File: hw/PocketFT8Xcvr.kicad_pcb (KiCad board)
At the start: 4 copper layers, 101.6 x 69.9 mm, 55 parts, among them IC1 SI5351C-B-GM1, J1 HX8357D SPI, J2 22-23-2021, J3 22-23-2021, J5 HX8357D 8-BIT, Q1 2N3904, Q2 2N3906, Q3 2N7000, Q4 2N7000, U1 MCP3422A1T-E/SN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

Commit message: Initial routing complete
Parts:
- moved C1 7.64 mm to (177.0, 62.5)
- moved C2 1.84 mm to (168.9, 69.5)
- moved R3 1.84 mm to (163.8, 69.2)
- moved C4 1.29 mm to (174.0, 62.5)
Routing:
- net /SDA: track 143.8 -> 177.4 mm, vias 5 -> 8
- net /SCL: track 110.7 -> 141.1 mm, vias 5 -> 8
- net Net-(U2-AMI): track 0.00 -> 27.9 mm, vias 0 -> 2
- net Net-(TN1-20_A6_TX5_LRCLK1): track 0.00 -> 26.6 mm, vias 0 -> 1
- net Net-(U2-LOUT/[DFS]): track 0.00 -> 21.1 mm, vias 0 -> 2
- net GND: track 97.5 -> 110.1 mm, vias 24 -> 29
- net +3.3V: track 66.1 -> 74.5 mm, vias 9 -> 11
- net Net-(U2-DBYP): track 0.00 -> 4.84 mm

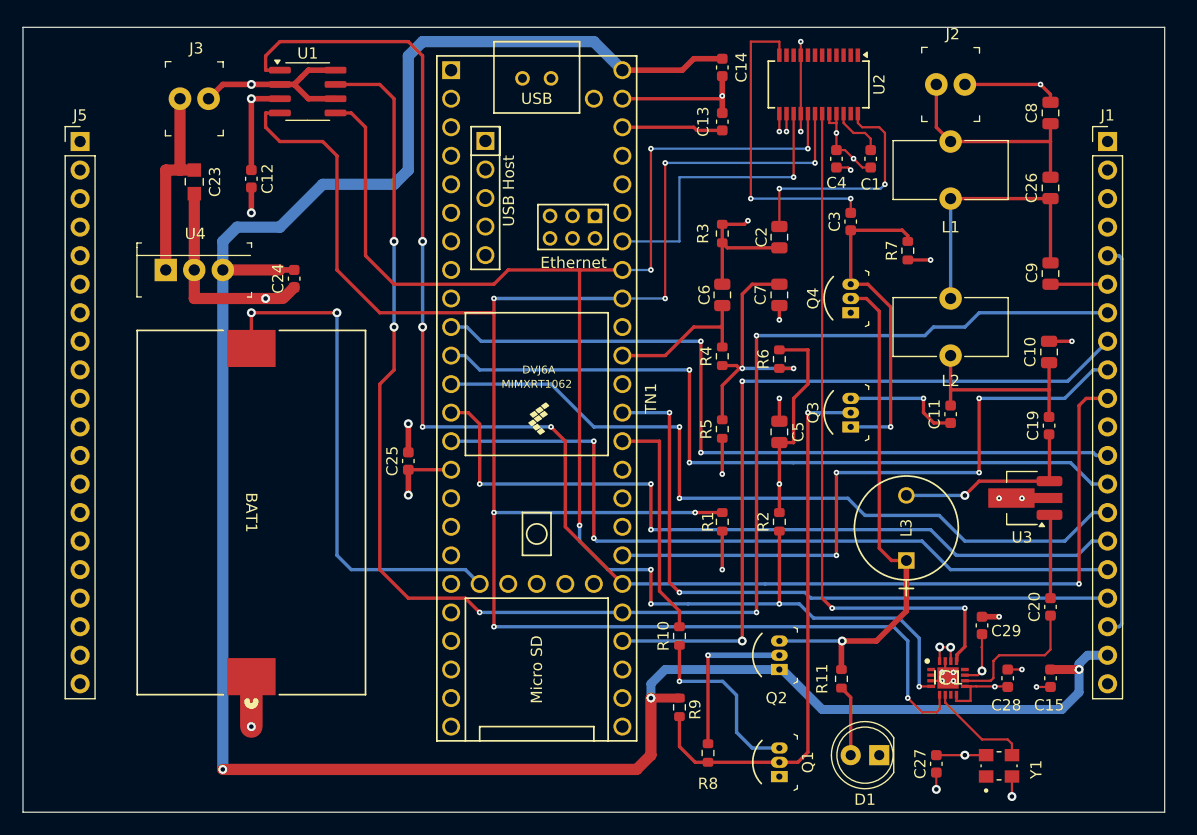
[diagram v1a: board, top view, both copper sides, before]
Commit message: Added GPS connector to board
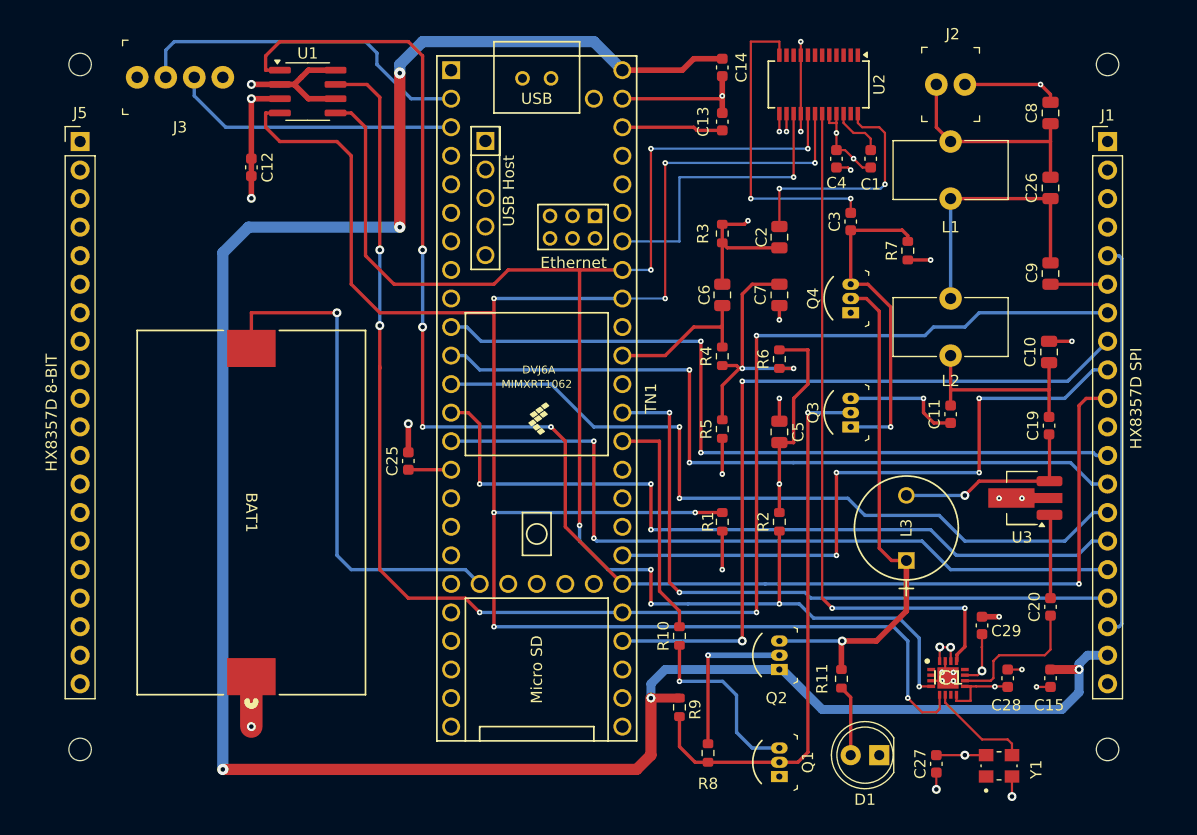
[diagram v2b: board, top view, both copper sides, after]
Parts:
- removed C23: 0.33UF, digikey-footprints:0805
- removed C24: 0.1UF, Capacitor_SMD:C_0603_1608Metric
- removed U4: L7805CV, digikey-footprints:TO-220-3
- added REF**: MountingHole_2mm, MountingHole:MountingHole_2mm, F.Cu at (106.7, 115.1)
- added REF**: MountingHole_2mm, MountingHole:MountingHole_2mm, F.Cu at (106.7, 54.1)
- added REF**: MountingHole_2mm, MountingHole:MountingHole_2mm, F.Cu at (198.1, 115.1)
- added REF**: MountingHole_2mm, MountingHole:MountingHole_2mm, F.Cu at (198.1, 54.1)
- J3: value 22-23-2021 -> GPS; footprint digikey-footprints:PinHeader_1x2_P2.54mm_Drill1.02mm -> digikey-footprints:PinHeader_1x4_P2.54mm_Drill1.02mm
- moved J3 4.26 mm to (111.8, 55.2)
- moved C12 1.02 mm to (121.9, 63.3)
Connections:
- J3 pad 1: +12V -> GND
- J3 pad 2: GND -> /GPSTX
- TN1 pad 2: unconnected-(TN1-0_RX1_CRX2_CS1-Pad2) -> /GPSTX
- TN1 pad 3: unconnected-(TN1-1_TX1_CTX2_MISO1-Pad3) -> /GPSRX
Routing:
- net /GPSTX: track 0.00 -> 30.8 mm
- net /GPSRX: track 0.00 -> 25.7 mm
- net GND: track 110.1 -> 85.3 mm, vias 29 -> 28
- net +12V: track 17.8 -> 0.00 mm
- net +5V: track 209.8 -> 204.1 mm, vias 3 -> 5
- net +3.3V: track 74.5 -> 72.4 mm, vias 11 -> 10
- net /X-: track 140.0 -> 138.4 mm
- net /SDA: track 177.4 -> 178.1 mm
- net Net-(TN1-VBAT): vias 2 -> 1
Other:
- board outline removed

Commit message: Review-1
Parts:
- added C16: 0.1UF, Capacitor_SMD:C_0603_1608Metric, F.Cu at (186.9, 97.5)
- added C17: 0.1UF, Capacitor_SMD:C_0603_1608Metric, F.Cu at (165.1, 111.5)
- moved C8 0.32 mm to (192.8, 58.6)
- moved C26 0.25 mm to (192.8, 65.1)
- moved C9 0.25 mm to (192.8, 72.7)
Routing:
- net /XMIT: track 46.4 -> 53.2 mm
- net GND: track 85.3 -> 81.8 mm, vias 28 -> 31
- net +5V: track 204.1 -> 206.9 mm, vias 5 -> 6
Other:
- board text added: "+3.3V"
- board text added: "+5V"
- board text added: "3V"
- board text added: "CS"
- board text added: "D/C"
- board text added: "DCK"
- board text added: "GND"
- board text added: "GPSRX"
- board text added: "GPSTX"
- board text added: "MSI"
- board text added: "MSO"
- board text added: "RST"
- board text added: "X+"
- board text added: "X-"
- board text added: "Y+"
- board text added: "Y-"

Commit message: Clean DRC
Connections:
- TN1 pad 48: +5V -> unconnected-(TN1-VIN-Pad48)
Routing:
- net +5V: track 206.9 -> 211.8 mm, vias 6 -> 7
- net Net-(C2-Pad2): track 10.8 -> 8.95 mm
- net GND: track 81.8 -> 80.7 mm
- net +3.3V: track 72.4 -> 71.3 mm
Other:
- board outline added: 101.6 x 69.9 mm
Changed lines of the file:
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@@
 	(net 104 "/GPSTX")
 	(net 105 "/GPSRX")
+	(net 106 "unconnected-(TN1-VIN-Pad48)")
 	(footprint "Capacitor_SMD:C_0603_1608Metric"
 		(layer "F.Cu")
@@
 			)
 		)
-		(fp_text user "DVJ6A"
-			(at -2.54 -0.18 0)
-			(layer "F.SilkS")
-			(effects
-				(font
-					(size 0.7 0.7)
-					(thickness 0.15)
-				)
-			)
-		)
 		(fp_text user "Ethernet"
 			(at -12.065 -3.2766 0)
@@
 			)
 		)
-		(fp_text user "MIMXRT1062"
-			(at -1.27 0 0)
-			(layer "F.SilkS")
-			(effects
-				(font
-					(size 0.7 0.7)
-					(thickness 0.15)
-				)
-			)
-		)
 		(pad "1" thru_hole rect
 			(at -29.21 7.62 270)
@@
 			(layers "*.Cu" "*.Mask")
 			(remove_unused_layers no)
-			(net 15 "+5V")
+			(net 106 "unconnected-(TN1-VIN-Pad48)")
 			(pinfunction "VIN")
-			(pintype "power_in")
+			(pintype "power_in+no_connect")
 		)
 		(pad "49" thru_hole circle
@@
 		(tags "Integrated Circuit")
 		(property "Reference" "IC1"
-			(at 0 0 0)
+			(at -0.278 -4.052 0)
 			(layer "F.SilkS")
 			(effects
@@
 		(sheetname "Root")
 		(sheetfile "PocketFT8Xcvr.kicad_sch")
+		(solder_mask_margin 0.1)
+		(clearance 0.1)
 		(attr smd)
 		(fp_circle
@@
 		(tags "RLB9012-102KL ")
 		(property "Reference" "L3"
-			(at -0.8128 -4.445 90)
+			(at 2.8956 0 90)
 			(unlocked yes)
 			(layer "F.SilkS")
@@
 		(tags "capacitor")
 		(property "Reference" "C26"
-			(at 0 -1.68 90)
+			(at 1.844 -1.778 90)
 			(layer "F.SilkS")
 			(effects
@@
 		(sheetname "Root")
 		(sheetfile "PocketFT8Xcvr.kicad_sch")
+		(solder_mask_margin 0.1)
+		(clearance 0.1)
 		(attr smd)
 		(fp_line
@@
 		)
 	)
+	(gr_rect
+		(start 101.6 50.8)
+		(end 203.2 120.65)
+		(stroke
+			(width 0.1)
+			(type default)
+		)
+		(fill none)
+		(layer "Edge.Cuts")
+	)
 	(gr_text "D/C"
 		(at 199.898 91.948 0)
@@
 	)
 	(segment
-		(start 128.27 57.15)
-		(end 129.41 57.15)
-		(width 0.3)
-		(layer "F.Cu")
-		(net 2)
-	)
-	(segment
 		(start 163.83 55.144)
 		(end 163.83 58.42)
@@
 	)
 	(segment
-		(start 186.8932 105.9688)
-		(end 186.944 105.918)
-		(width 0.2)
-		(layer "F.Cu")
-		(net 3)
-	)
-	(segment
 		(start 170.18 83.82)
 		(end 170.18 87.757)
@@
 	)
 	(segment
-		(start 121.92 57.15)
-		(end 121.92 63.5)
-		(width 0.5)
-		(layer "F.Cu")
-		(net 3)
-	)
-	(segment
 		(start 175.514 62.484)
 		(end 174.752 61.722)
@@
 		(net 3)
 	)
+	(segment
+		(start 121.92 57.15)
+		(end 121.92 62.484)
+		(width 0.5)
+		(layer "F.Cu")
+		(net 3)
+	)
 	(via
 		(at 186.944 108.077)
@@
 	)
 	(segment
-		(start 163.83 73.66)
-		(end 163.83 68.135)
+		(start 168.91 70.421)
+		(end 164.275 70.421)
 		(width 0.3)
 		(layer "F.Cu")
@@
 	)
 	(segment
-		(start 168.91 70.421)
-		(end 164.275 70.421)
-		(width 0.3)
+		(start 163.83 73.66)
+		(end 163.83 69.976)
+		(width 0.25)
 		(layer "F.Cu")
 		(net 5)
@@
 	)
 	(segment
-		(start 175.26 67.31)
-		(end 175.26 66.04)
+		(start 168.91 52.324)
+		(end 168.656 52.07)
 		(width 0.2)
 		(layer "F.Cu")
@@
 	)
 	(segment
-		(start 166.37 52.07)
+		(start 166.37 52.324)
 		(end 166.37 66.04)
 		(width 0.2)
@@
 	)
 	(segment
-		(start 168.91 52.07)
-		(end 166.37 52.07)
+		(start 175.26 67.31)
+		(end 175.26 66.04)
+		(width 0.2)
+		(layer "F.Cu")
+		(net 8)
+	)
+	(segment
+		(start 166.624 52.07)
+		(end 166.37 52.324)
 		(width 0.2)
 		(layer "F.Cu")
@@
 	(segment
 		(start 168.91 53.28)
-		(end 168.91 52.07)
+		(end 168.91 52.324)
+		(width 0.2)
+		(layer "F.Cu")
+		(net 8)
+	)
+	(segment
+		(start 168.656 52.07)
+		(end 166.624 52.07)
 		(width 0.2)
 		(layer "F.Cu")
@@
 	)
 	(segment
-		(start 182.652 86.005)
-		(end 184.15 86.005)
+		(start 184.15 86.005)
+		(end 182.652 86.005)
 		(width 0.3)
 		(layer "F.Cu")
@@
 	)
 	(segment
-		(start 135.128 68.58)
-		(end 135.128 54.864)
+		(start 157.734 51.816)
+		(end 152.4 51.816)
 		(width 1)
 		(layer "F.Cu")
@@
 	)
 	(segment
-		(start 161.29 53.594)
-		(end 163.83 53.594)
-		(width 0.8)
+		(start 135.128 68.58)
+		(end 135.128 54.864)
+		(width 1)
 		(layer "F.Cu")
 		(net 15)
@@
 	)
 	(segment
+		(start 152.4 51.816)
+		(end 152.146 51.816)
+		(width 1)
+		(layer "F.Cu")
+		(net 15)
+	)
+	(segment
 		(start 193.04 107.95)
 		(end 195.326 107.95)
@@
 	)
 	(segment
-		(start 154.94 54.61)
-		(end 160.274 54.61)
-		(width 0.8)
+		(start 159.512 53.594)
+		(end 157.734 51.816)
+		(width 1)
 		(layer "F.Cu")
 		(net 15)
@@
 	)
 	(segment
-		(start 160.274 54.61)
-		(end 161.29 53.594)
-		(width 0.8)
+		(start 163.83 53.594)
+		(end 159.512 53.594)
+		(width 1)
 		(layer "F.Cu")
 		(net 15)
@@
 		(net 15)
 	)
+	(via
+		(at 152.4 51.816)
+		(size 0.8)
+		(drill 0.4)
+		(layers "F.Cu" "B.Cu")
+		(net 15)
+	)
 	(segment
 		(start 168.91 107.95)
@@
 	)
 	(segment
+		(start 152.4 57.15)
+		(end 152.4 51.816)
+		(width 1)
+		(layer "B.Cu")
+		(net 15)
+	)
+	(segment
 		(start 119.38 116.84)
 		(end 119.38 70.866)
@@
 	)
 	(segment
-		(start 152.4 52.07)
-		(end 137.16 52.07)
-		(width 1)
-		(layer "B.Cu")
-		(net 15)
-	)
-	(segment
 		(start 196.342 106.68)
 		(end 198.12 106.68)
@@
 	)
 	(segment
-		(start 154.94 54.61)
-		(end 152.4 52.07)
-		(width 1)
+		(start 165.1 107.95)
+		(end 158.75 107.95)
+		(width 0.8)
 		(layer "B.Cu")
 		(net 15)
 	)
 	(segment
-		(start 165.1 107.95)
-		(end 158.75 107.95)
-		(width 0.8)
+		(start 152.4 51.816)
+		(end 137.414 51.816)
+		(width 1)
 		(layer "B.Cu")
 		(net 15)
@@
 	)
 	(segment
-		(start 137.16 52.07)
+		(start 137.414 51.816)
 		(end 135.128 54.102)
 		(width 1)
@@
 	)
 	(segment
+		(start 135.128 54.102)
+		(end 135.128 54.864)
+		(width 1)
+		(layer "B.Cu")
+		(net 15)
+	)
+	(segment
 		(start 194.056 111.506)
 		(end 195.58 109.982)
@@
 	)
 	(segment
-		(start 135.128 54.102)
-		(end 135.128 54.864)
-		(width 1)
-		(layer "B.Cu")
-		(net 15)
-	)
-	(segment
 		(start 187.96 107.188)
 		(end 188.468 106.68)
@@
 		(width 0.3)
 		(layer "B.Cu")
-		(net 97)
-	)
-	(segment
-		(start 170.053 89.535)
-		(end 170.18 89.535)
-		(width 0.3)
-		(layer "B.Cu")

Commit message: Minor cleanup
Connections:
- TN1 pad 51: unconnected-(TN1-3V3-Pad51) -> +3.3V
- TN1 pad 52: unconnected-(TN1-GND-Pad52) -> GND
